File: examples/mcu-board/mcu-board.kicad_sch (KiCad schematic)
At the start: 11 parts, among them J1 5V_IN, J2 PROG/IO, SW1 Reset, U1 MCU, U2 AMS1117-3.3

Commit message: examples/mcu-board: lay out for expansion (regions, spare GPIO, GND fan)
Iteration on the mcu-board example so it works as a "real board you'd
extend" rather than a one-shot snapshot. Three concrete changes:

Schematic — break out every spare MCU GPIO (PA1, PA2, PA3, PA5) as a
named-net label stub at the MCU pin. Adding a peripheral later means
dropping in a component with a label on the matching net; no rerouting
of existing wires.

PCB — redo the layout with three named silkscreen regions
("POWER" / "MCU" / "PERIPHERALS") matching the left-to-right power
flow, on a larger 80×50 mm board. The bottom-third of the board is
intentionally left empty (silkscreen "expansion" marker) so an
added peripheral can land somewhere with mounting holes still
unobstructed at the corners.

PCB — replace the old single-segment B.Cu trace with a fan of GND
drops from each GND-bearing pad to a horizontal spine at the bottom
edge. kicad-cli can't compute zone fills offline, so this is the
closest we can get to "looks like a real GND pour" while staying
fully renderable from the CLI.

Co-Authored-By: Claude Opus 4.7 (1M context) <noreply@anthropic.com>
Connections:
- net PA1: now also U1.2 (PA1)
- net PA2: now also U1.3 (PA2)
- net PA3: now also U1.6 (PA3)
- net PA5: now reaches U1.8 (PA5)

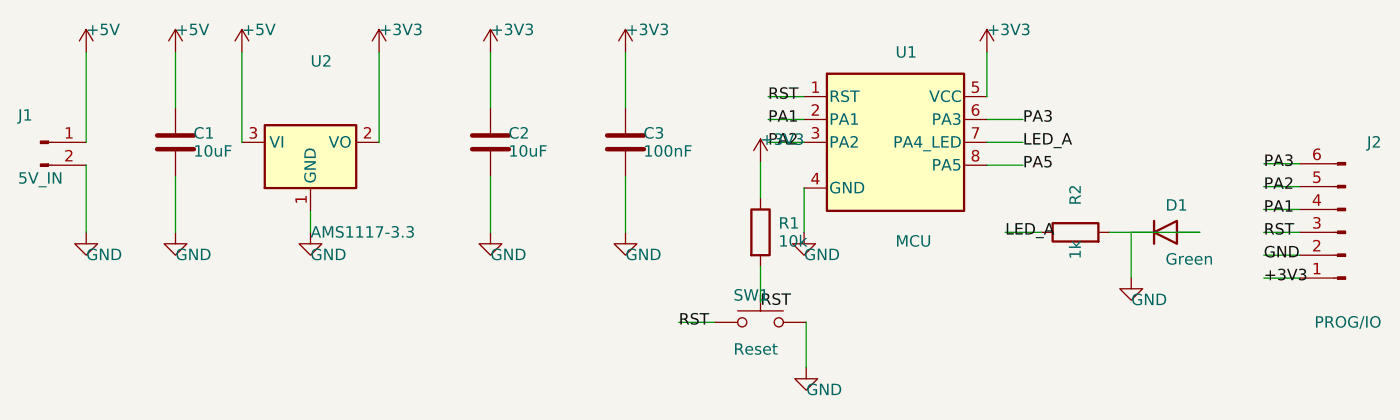
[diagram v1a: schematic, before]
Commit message: examples/mcu-board: polish silkscreen / label placement
Render-feedback driven cleanup of the previous layout pass:

- "PERIPHERALS" silkscreen overflowed the right board edge → renamed
  to "I/O" and the region X positions are pre-computed to centre each
  label on its zone (kicad-cli rejects `(justify center)` on top-level
  gr_text, so all silkscreen text is left-justified).
- J1's value ("5V_IN") was rendered off the *left* board edge because
  its silkscreen labels were always on the connector's left side. The
  fp_header helper now takes a `side="left"|"right"` arg; J1 (near
  the left edge) uses `side="right"`, J2 (near the right edge) keeps
  the default `side="left"`. Both ref and value sit on the same side.
- SW1 ("Reset") and R2 ("1k") collided on the silkscreen because their
  text positions happened to coincide. R2 + D1 moved one row down, so
  the reset network gets the upper peripheral row to itself.
- Schematic stubs from MCU pins to named-net labels were 4 mm long;
  bumped to 6 mm so the label glyphs no longer crowd the pin-number
  glyphs at the symbol edge.

Co-Authored-By: Claude Opus 4.7 (1M context) <noreply@anthropic.com>
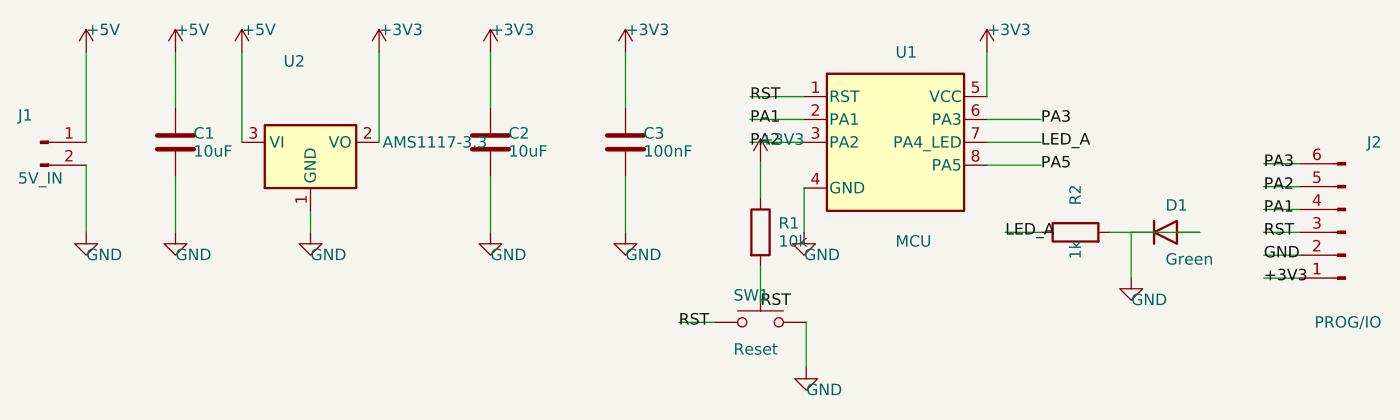
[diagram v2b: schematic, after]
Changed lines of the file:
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@@
 		(at 80 85 0)
 		(unit 1)
-		(property "Reference" "U2" (at 80 76 0) (effects (font (size 1.27 1.27)) (justify left)))
-		(property "Value" "AMS1117-3.3" (at 80 95 0) (effects (font (size 1.27 1.27)) (justify left)))
+		(property "Reference" "U2" (at 77 76 0) (effects (font (size 1.27 1.27)) (justify left)))
+		(property "Value" "AMS1117-3.3" (at 88 85 0) (effects (font (size 1.27 1.27)) (justify left)))
 		(instances (project "mcu-board"
 			(path "/10000000-0000-0000-0000-000000000001" (reference "U2") (unit 1))))
@@
 		(stroke (width 0) (type default))
 )
-	(wire (pts (xy 134.84 79.92) (xy 130.84 79.92))
-		(stroke (width 0) (type default))
-)
-	(wire (pts (xy 155.16 85) (xy 159.16 85))
-		(stroke (width 0) (type default))
-)
-	(wire (pts (xy 134.84 82.46) (xy 130.84 82.46))
-		(stroke (width 0) (type default))
-)
-	(wire (pts (xy 134.84 85) (xy 130.84 85))
-		(stroke (width 0) (type default))
-)
-	(wire (pts (xy 155.16 82.46) (xy 159.16 82.46))
-		(stroke (width 0) (type default))
-)
-	(wire (pts (xy 155.16 87.54) (xy 159.16 87.54))
+	(wire (pts (xy 134.84 79.92) (xy 128.84 79.92))
+		(stroke (width 0) (type default))
+)
+	(wire (pts (xy 155.16 85) (xy 161.16 85))
+		(stroke (width 0) (type default))
+)
+	(wire (pts (xy 134.84 82.46) (xy 128.84 82.46))
+		(stroke (width 0) (type default))
+)
+	(wire (pts (xy 134.84 85) (xy 128.84 85))
+		(stroke (width 0) (type default))
+)
+	(wire (pts (xy 155.16 82.46) (xy 161.16 82.46))
+		(stroke (width 0) (type default))
+)
+	(wire (pts (xy 155.16 87.54) (xy 161.16 87.54))
 		(stroke (width 0) (type default))
 )
@@
 		(stroke (width 0) (type default))
 )
-	(label "RST" (at 130.84 79.92 0) (effects (font (size 1.27 1.27)) (justify left)))
+	(label "RST" (at 128.84 79.92 0) (effects (font (size 1.27 1.27)) (justify left)))
 	(label "RST" (at 130 102.81 0) (effects (font (size 1.27 1.27)) (justify left)))
 	(label "RST" (at 120.92 105 0) (effects (font (size 1.27 1.27)) (justify left)))
-	(label "LED_A" (at 159.16 85 0) (effects (font (size 1.27 1.27)) (justify left)))
+	(label "LED_A" (at 161.16 85 0) (effects (font (size 1.27 1.27)) (justify left)))
 	(label "LED_A" (at 157.19 95 0) (effects (font (size 1.27 1.27)) (justify left)))
-	(label "PA1" (at 130.84 82.46 0) (effects (font (size 1.27 1.27)) (justify left)))
-	(label "PA2" (at 130.84 85 0) (effects (font (size 1.27 1.27)) (justify left)))
-	(label "PA3" (at 159.16 82.46 0) (effects (font (size 1.27 1.27)) (justify left)))
-	(label "PA5" (at 159.16 87.54 0) (effects (font (size 1.27 1.27)) (justify left)))
+	(label "PA1" (at 128.84 82.46 0) (effects (font (size 1.27 1.27)) (justify left)))
+	(label "PA2" (at 128.84 85 0) (effects (font (size 1.27 1.27)) (justify left)))
+	(label "PA3" (at 161.16 82.46 0) (effects (font (size 1.27 1.27)) (justify left)))
+	(label "PA5" (at 161.16 87.54 0) (effects (font (size 1.27 1.27)) (justify left)))
 	(wire (pts (xy 189.92 100.08) (xy 185.92 100.08))
 		(stroke (width 0) (type default))
